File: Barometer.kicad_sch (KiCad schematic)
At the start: 0 parts

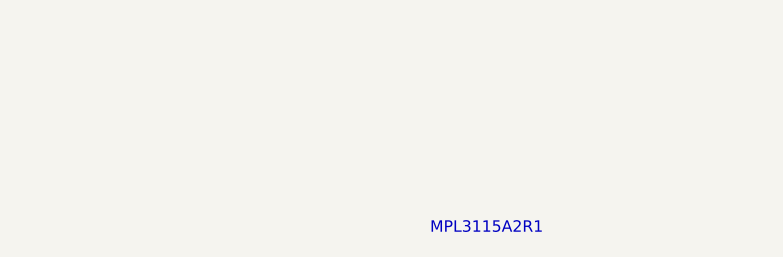
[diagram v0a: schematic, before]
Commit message: began fixing schematic added barometer
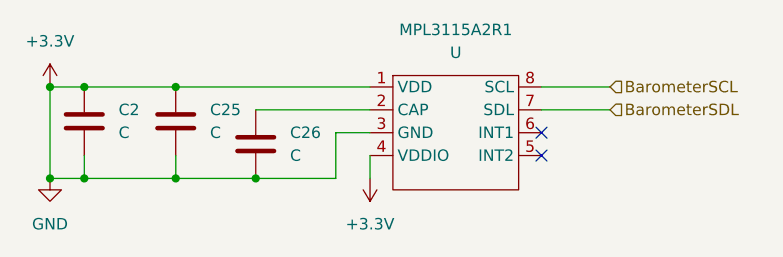
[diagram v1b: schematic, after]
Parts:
- added C2, C25, C26: C, symbol Device:C
- added MPL3115A2R1: U, symbol Footprints:MPL3115A2R1
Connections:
- new net: C26.1, MPL3115A2R1.2 (CAP)
- new net +3.3V: C2.1, C2.2, C25.1, C25.2, C26.2, MPL3115A2R1.1 (VDD), MPL3115A2R1.3 (GND), MPL3115A2R1.4 (VDDIO)
- new net BarometerSCL: MPL3115A2R1.8 (SCL)
- new net BarometerSDL: MPL3115A2R1.7 (SDL)
- no-connect marks 0 -> 2
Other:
- note removed: "MPL3115A2R1"
